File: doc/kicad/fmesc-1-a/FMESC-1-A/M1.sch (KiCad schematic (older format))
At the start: 22 parts, among them J1 Conn_01x02, J2 Conn_01x02, J3 Conn_01x02, J4 Conn_01x02, J5 Conn_01x02, J6 Conn_01x02, Q1 AON6504, Q2 AON6504, Q3 AON6504, Q4 AON6504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

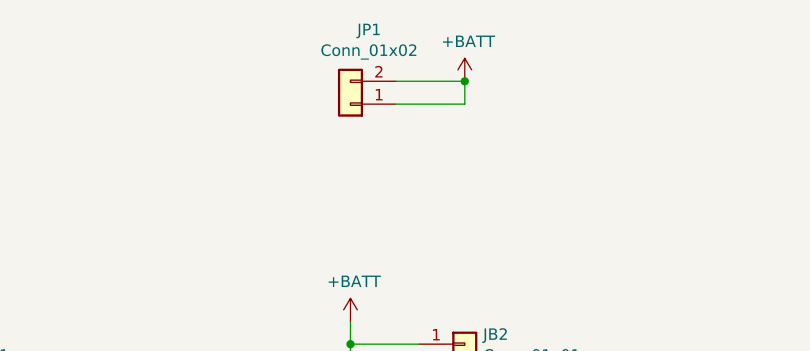
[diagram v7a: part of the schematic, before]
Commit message: doc/kicad: FMESC-1-A PCB finish layout
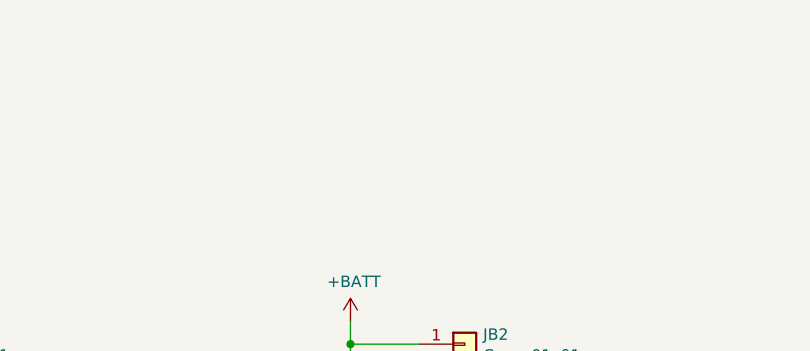
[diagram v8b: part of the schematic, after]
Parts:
- removed JP1: Conn_01x02, fmlibf:JS_2P_1.0mm, symbol Connector_Generic:Conn_01x02
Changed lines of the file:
@@
 	1    0    0    -1
 $EndComp
-$Comp
-L Connector_Generic:Conn_01x02 JP1
-U 1 1 5FA90D52
-P 5000 3550
-AR Path="/5FA1845D/5FA90D52" Ref="JP1"  Part="1"
-AR Path="/5FA3E74F/5FA90D52" Ref="JP2"  Part="1"
-AR Path="/5FA3EBFA/5FA90D52" Ref="JP3"  Part="1"
-AR Path="/5FA3F05C/5FA90D52" Ref="JP4"  Part="1"
-F 0 "JP1" H 4918 3225 50  0000 C CNN
-F 1 "Conn_01x02" H 4918 3316 50  0000 C CNN
-F 2 "fmlibf:JS_2P_1.0mm" H 5000 3550 50  0001 C CNN
-F 3 "~" H 5000 3550 50  0001 C CNN
-	1    5000 3550
-	-1   0    0    1
-$EndComp
-$Comp
-L power:+BATT #PWR0142
-U 1 1 5FA91FDD
-P 5500 3450
-AR Path="/5FA1845D/5FA91FDD" Ref="#PWR0142"  Part="1"
-AR Path="/5FA3E74F/5FA91FDD" Ref="#PWR0138"  Part="1"
-AR Path="/5FA3EBFA/5FA91FDD" Ref="#PWR0134"  Part="1"
-AR Path="/5FA3F05C/5FA91FDD" Ref="#PWR0118"  Part="1"
-F 0 "#PWR0142" H 5500 3300 50  0001 C CNN
-F 1 "+BATT" H 5515 3623 50  0000 C CNN
-F 2 "" H 5500 3450 50  0001 C CNN
-F 3 "" H 5500 3450 50  0001 C CNN
-	1    5500 3450
-	1    0    0    -1
-$EndComp
-Wire Wire Line
-	5200 3550 5500 3550
-Wire Wire Line
-	5500 3550 5500 3450
-Wire Wire Line
-	5500 3450 5200 3450
-Connection ~ 5500 3450
 $EndSCHEMATC
